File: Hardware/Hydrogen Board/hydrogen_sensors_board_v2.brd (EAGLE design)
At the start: 68.2 x 66 mm, 39 parts, among them U1 ATMEGA328P_TQFP, Y1 16MHz

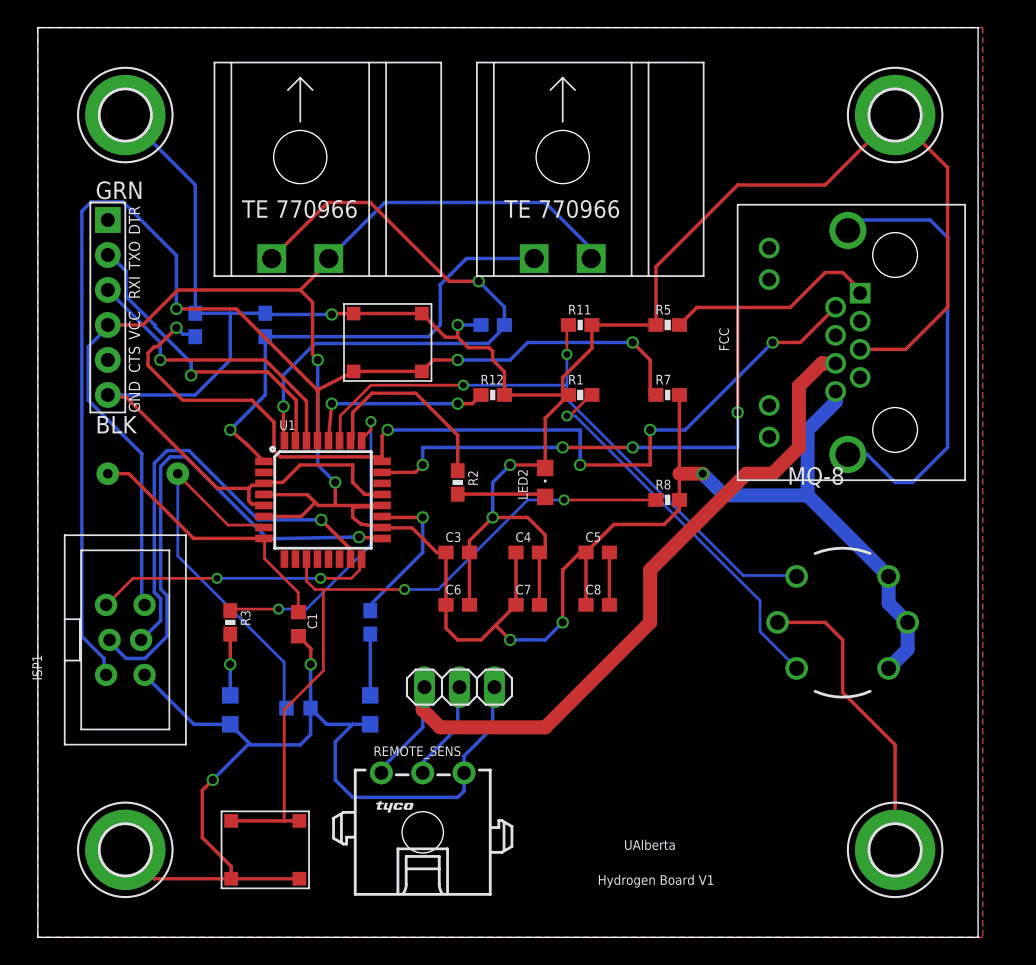
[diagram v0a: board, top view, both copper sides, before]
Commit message: got rid of redundant ground traces
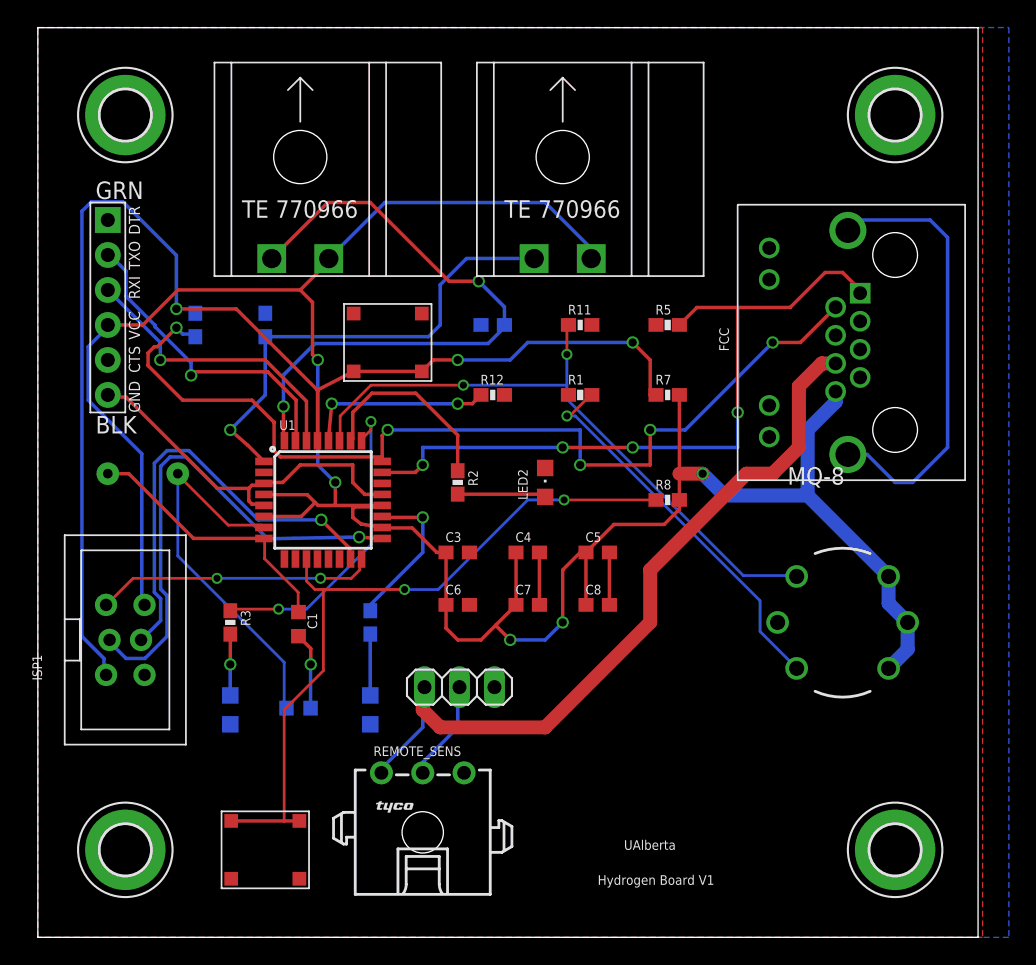
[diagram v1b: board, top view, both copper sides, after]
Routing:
- net GND: track 281.6 -> 40.4 mm, vias 6 -> 1

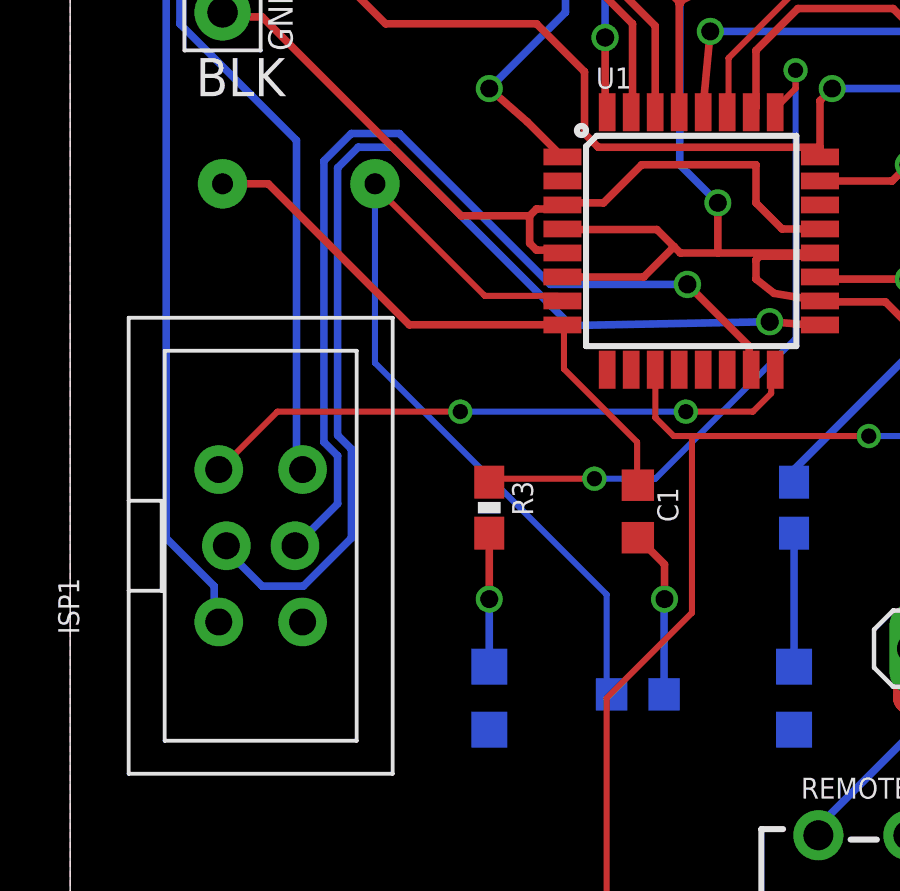
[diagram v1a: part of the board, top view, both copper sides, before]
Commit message: removed more useless ground traces. Moved caps for xtal closer to the actual crystal
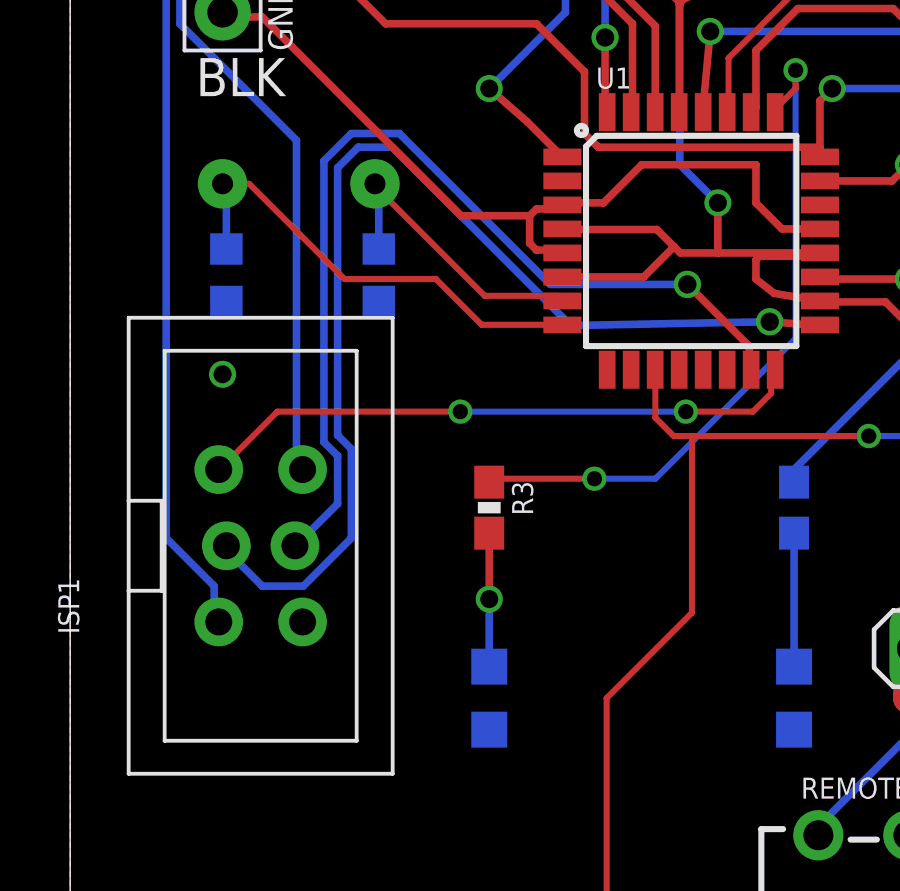
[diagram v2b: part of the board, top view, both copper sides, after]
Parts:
- moved C2 16.4 mm to (10.3, 30.6), turned to 270 degrees
- moved C1 15.8 mm to (5.21, 30.6), flipped to the bottom
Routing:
- net N$1: track 28.2 -> 10.1 mm
- net GND: track 40.4 -> 34.8 mm
- net N$3: track 19.7 -> 15.5 mm
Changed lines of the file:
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@@
 <setting verticaltext="up"/>
 </settings>
-<grid distance="0.025" unitdist="inch" unit="inch" style="lines" multiple="1" display="no" altdistance="0.005" altunitdist="inch" altunit="inch"/>
+<grid distance="0.02" unitdist="inch" unit="inch" style="lines" multiple="1" display="no" altdistance="0.005" altunitdist="inch" altunit="inch"/>
 <layers>
 <layer number="1" name="Top" color="4" fill="1" visible="yes" active="yes"/>
@@
 </autorouter>
 <elements>
-<element name="C1" library="adafruit" package="C0603K" value="22pF" x="18.923" y="22.733" smashed="yes" rot="R270">
-<attribute name="NAME" x="19.573" y="23.533" size="0.7" layer="25" ratio="15" rot="R270"/>
-</element>
-<element name="C2" library="adafruit" package="C0603K" value="22pF" x="18.923" y="16.637" smashed="yes" rot="MR180">
-<attribute name="NAME" x="18.123" y="15.987" size="0.7" layer="26" ratio="15" rot="MR180"/>
+<element name="C1" library="adafruit" package="C0603K" value="22pF" x="5.207" y="30.607" smashed="yes" rot="MR270">
+<attribute name="NAME" x="4.557" y="31.407" size="0.7" layer="26" ratio="15" rot="MR270"/>
+</element>
+<element name="C2" library="adafruit" package="C0603K" value="22pF" x="10.287" y="30.607" smashed="yes" rot="MR270">
+<attribute name="NAME" x="9.637" y="31.407" size="0.7" layer="26" ratio="15" rot="MR270"/>
 </element>
 <element name="ETH1" library="ETHERNET" package="A122645-ND" value="FCC" x="62.23" y="43.18" smashed="yes" rot="R90">
@@
 <contactref element="C3" pad="2"/>
 <wire x1="41.49" y1="27.94" x2="41.49" y2="24.13" width="0.254" layer="1"/>
-<wire x1="19.798" y1="16.637" x2="19.798" y2="19.798" width="0.254" layer="16"/>
-<wire x1="19.798" y1="19.798" x2="19.812" y2="19.812" width="0.254" layer="16"/>
-<via x="19.812" y="19.812" extent="1-16" drill="0.6"/>
-<wire x1="19.812" y1="19.812" x2="19.812" y2="20.969" width="0.254" layer="1"/>
-<wire x1="19.812" y1="20.969" x2="18.923" y2="21.858" width="0.254" layer="1"/>
 <wire x1="36.41" y1="24.13" x2="36.41" y2="27.94" width="0.254" layer="1"/>
 <polygon width="0.4064" layer="1" isolate="0.3048">
@@
 <vertex x="70.485" y="0"/>
 </polygon>
-<wire x1="59.69" y1="42.68" x2="62.23" y2="59.69" width="0" layer="19" extent="1-1"/>
-<wire x1="44.87" y1="44.45" x2="59.69" y2="42.68" width="0" layer="19" extent="1-1"/>
-<wire x1="40.22" y1="44.45" x2="44.87" y2="44.45" width="0" layer="19" extent="1-1"/>
-<wire x1="38.52" y1="39.37" x2="40.22" y2="44.45" width="0" layer="19" extent="1-1"/>
-<wire x1="33.87" y1="39.37" x2="38.52" y2="39.37" width="0" layer="19" extent="1-1"/>
-<wire x1="32.17" y1="44.45" x2="33.87" y2="39.37" width="0" layer="19" extent="1-16"/>
-<wire x1="27.875" y1="45.28" x2="32.17" y2="44.45" width="0" layer="19" extent="1-16"/>
-<wire x1="22.925" y1="45.28" x2="27.875" y2="45.28" width="0" layer="19" extent="1-1"/>
-<wire x1="36.83" y1="34.07" x2="38.52" y2="39.37" width="0" layer="19" extent="1-1"/>
-<wire x1="36.41" y1="27.94" x2="36.83" y2="34.07" width="0" layer="19" extent="1-1"/>
-<wire x1="41.49" y1="27.94" x2="36.41" y2="27.94" width="0" layer="19" extent="1-1"/>
-<wire x1="31.33" y1="27.94" x2="36.41" y2="27.94" width="0" layer="19" extent="1-1"/>
-<wire x1="31.33" y1="24.13" x2="31.33" y2="27.94" width="0" layer="19" extent="1-1"/>
-<wire x1="33.147" y1="18.161" x2="31.33" y2="24.13" width="0" layer="19" extent="1-1"/>
-<wire x1="16.51" y1="45.3" x2="22.925" y2="45.28" width="0" layer="19" extent="1-16"/>
-<wire x1="11.43" y1="45.3" x2="16.51" y2="45.3" width="0" layer="19" extent="16-16"/>
-<wire x1="30.94" y1="11.94" x2="33.147" y2="18.161" width="0" layer="19" extent="1-1"/>
-<wire x1="24.9936" y1="32.15" x2="31.33" y2="27.94" width="0" layer="19" extent="1-1"/>
-<wire x1="24.13" y1="15.46" x2="30.94" y2="11.94" width="0" layer="19" extent="16-16"/>
-<wire x1="19.798" y1="16.637" x2="24.13" y2="15.46" width="0" layer="19" extent="16-16"/>
-<wire x1="13.97" y1="15.46" x2="19.798" y2="16.637" width="0" layer="19" extent="16-16"/>
-<wire x1="7.747" y1="19.05" x2="13.97" y2="15.46" width="0" layer="19" extent="16-16"/>
-<wire x1="14.035" y1="4.25" x2="13.97" y2="15.46" width="0" layer="19" extent="1-16"/>
-<wire x1="18.985" y1="4.25" x2="14.035" y2="4.25" width="0" layer="19" extent="1-1"/>
-<wire x1="6.35" y1="6.35" x2="14.035" y2="4.25" width="0" layer="19" extent="1-1"/>
-<wire x1="53.7" y1="22.86" x2="41.49" y2="24.13" width="0" layer="19" extent="1-1"/>
-<wire x1="6.35" y1="59.69" x2="11.43" y2="45.3" width="0" layer="19" extent="16-16"/>
-<wire x1="62.23" y1="6.35" x2="53.7" y2="22.86" width="0" layer="19" extent="1-1"/>
+<via x="5.08" y="27.305" extent="1-16" drill="0.6" diameter="0.75"/>
 </signal>
 <signal name="N$2">
@@
 <contactref element="U1" pad="7"/>
 <contactref element="C2" pad="1"/>
-<wire x1="17.8816" y1="19.9644" x2="17.8816" y2="16.7132" width="0.2032" layer="16"/>
-<wire x1="10.16" y1="27.686" x2="17.8816" y2="19.9644" width="0.2032" layer="16"/>
-<wire x1="10.16" y1="33.655" x2="10.16" y2="27.686" width="0.2032" layer="16"/>
-<wire x1="17.8816" y1="16.7132" x2="18.048" y2="16.637" width="0.2032" layer="16"/>
 <wire x1="13.8176" y1="29.9212" x2="16.256" y2="29.9212" width="0.2032" layer="1"/>
 <wire x1="10.16" y1="33.5788" x2="13.8176" y2="29.9212" width="0.2032" layer="1"/>
 <wire x1="16.256" y1="29.9212" x2="16.4084" y2="29.75" width="0.2032" layer="1"/>
 <wire x1="10.16" y1="33.5788" x2="10.16" y2="33.655" width="0.2032" layer="1"/>
+<wire x1="10.287" y1="31.482" x2="10.287" y2="33.528" width="0.254" layer="16"/>
+<wire x1="10.287" y1="33.528" x2="10.16" y2="33.655" width="0.254" layer="16"/>
 </signal>
 <signal name="N$3">
@@
 <contactref element="Y1" pad="1"/>
 <contactref element="C1" pad="1"/>
-<wire x1="5.08" y1="33.655" x2="6.604" y2="33.655" width="0.254" layer="1"/>
-<wire x1="6.604" y1="33.655" x2="11.303" y2="28.956" width="0.254" layer="1"/>
-<wire x1="11.303" y1="28.956" x2="16.4024" y2="28.956" width="0.254" layer="1"/>
-<wire x1="16.4024" y1="28.956" x2="16.4084" y2="28.95" width="0.254" layer="1"/>
-<wire x1="18.8976" y1="25.0444" x2="18.8976" y2="23.622" width="0.2032" layer="1"/>
-<wire x1="16.4592" y1="27.4828" x2="18.8976" y2="25.0444" width="0.2032" layer="1"/>
-<wire x1="16.4592" y1="28.9052" x2="16.4592" y2="27.4828" width="0.2032" layer="1"/>
-<wire x1="18.8976" y1="23.622" x2="18.923" y2="23.608" width="0.2032" layer="1"/>
-<wire x1="16.4592" y1="28.9052" x2="16.4084" y2="28.95" width="0.2032" layer="1"/>
+<wire x1="5.207" y1="31.482" x2="5.207" y2="33.528" width="0.254" layer="16"/>
+<wire x1="5.207" y1="33.528" x2="5.08" y2="33.655" width="0.254" layer="16"/>
+<wire x1="5.08" y1="33.655" x2="5.969" y2="33.655" width="0.2032" layer="1"/>
+<wire x1="5.969" y1="33.655" x2="9.144" y2="30.48" width="0.2032" layer="1"/>
+<wire x1="9.144" y1="30.48" x2="12.192" y2="30.48" width="0.2032" layer="1"/>
+<wire x1="12.192" y1="30.48" x2="13.716" y2="28.956" width="0.2032" layer="1"/>
+<wire x1="13.716" y1="28.956" x2="16.4024" y2="28.956" width="0.2032" layer="1"/>
+<wire x1="16.4024" y1="28.956" x2="16.4084" y2="28.95" width="0.2032" layer="1"/>
 </signal>
 <signal name="ATM_RESET">

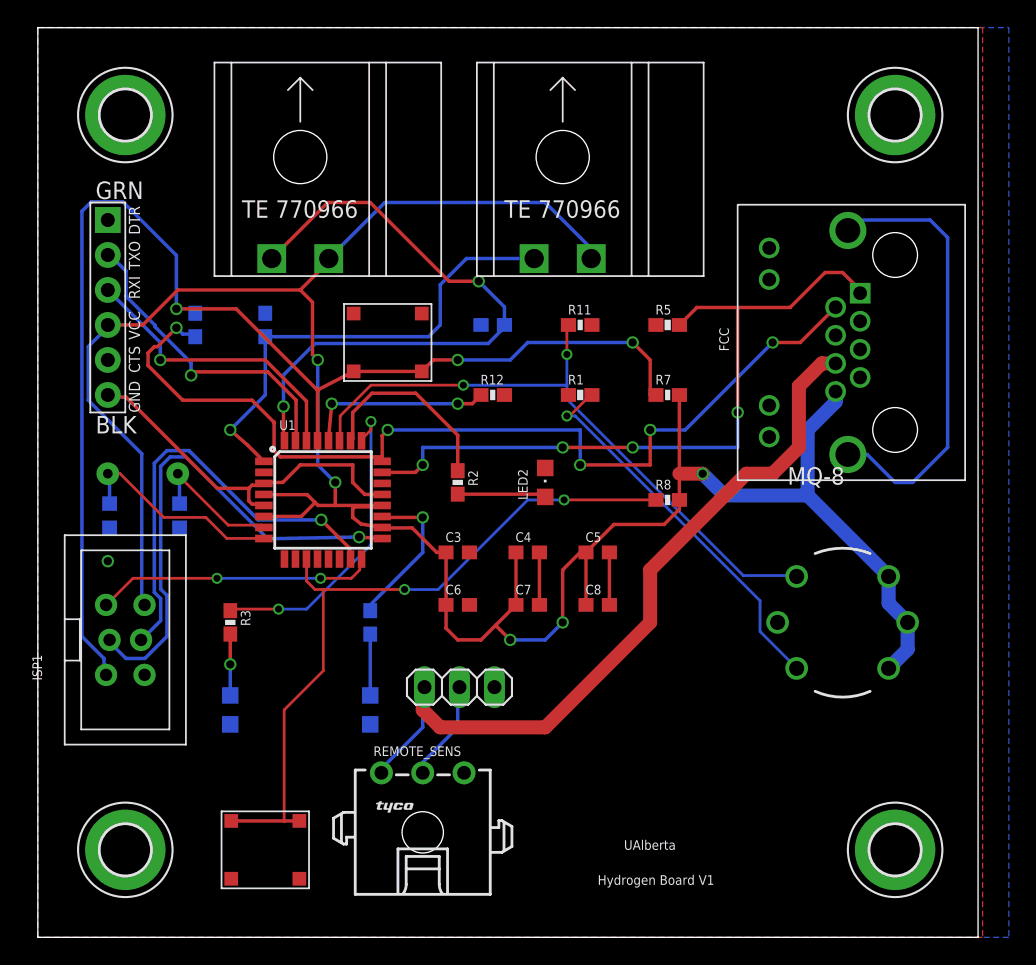
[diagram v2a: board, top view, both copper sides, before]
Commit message: more general clean up. Moved LEDs to top layer. Removed some useless traces. Fixed warnings
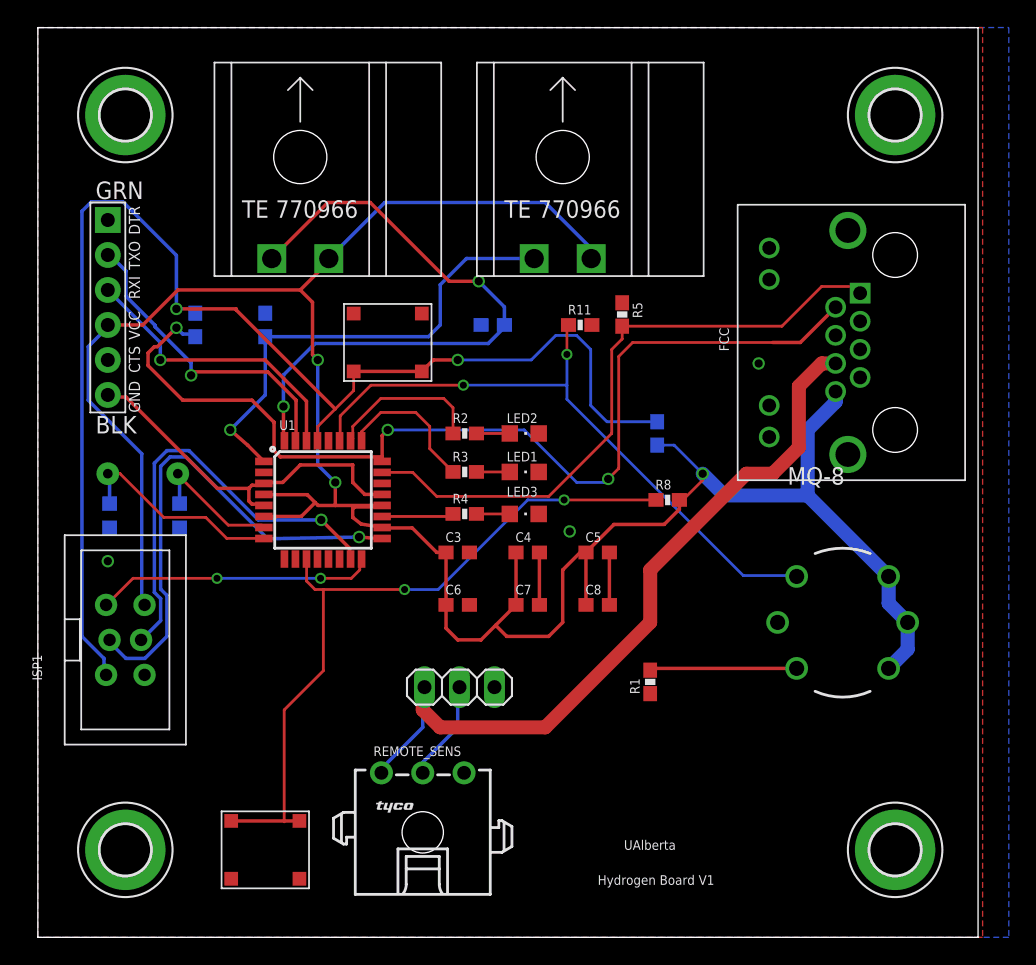
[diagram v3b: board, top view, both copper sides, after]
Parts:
- removed R12: 100k, SparkFun-Resistors:0603-RES
- moved LED1 27.5 mm to (35.3, 33.8), flipped to the top, turned to 270 degrees
- moved R1 21.4 mm to (44.5, 18.5), turned to 90 degrees
- moved R3 20.2 mm to (31.0, 33.8), turned to 0 degrees
- moved LED3 18.1 mm to (35.3, 30.7), flipped to the top, turned to 270 degrees
- moved R4 10.4 mm to (31.0, 30.7), flipped to the top, turned to 0 degrees
- moved LED2 3.87 mm to (35.3, 36.6), turned to 270 degrees
- moved R2 3.59 mm to (31.0, 36.6), turned to 0 degrees
- moved R5 3.39 mm to (42.4, 45.2), turned to 270 degrees
- moved R7 2.90 mm to (45.0, 36.6), flipped to the bottom, turned to 270 degrees
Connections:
- removed net H2OUT_2: R12.1, U1.28
- removed net N$10: ETH1.P$13, ETH1.P$14
- removed net N$16: ETH1.P$3
- removed net N$22: ETH1.P$10
- removed net N$23: ETH1.P$9
- removed net N$24: ETH1.P$12
- removed net N$25: ETH1.P$11
- net GND: now also ETH1.P$13, ETH1.P$14; no longer R12.2
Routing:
- net N$10: track 32.5 -> 0.00 mm
- net N$2: track 28.0 -> 10.7 mm, vias 1 -> 0
- net H2OUT_2: track 13.8 -> 0.00 mm, vias 2 -> 0
- net N$4: track 22.8 -> 10.6 mm, vias 2 -> 0
- net H2_OK: track 52.9 -> 46.0 mm, vias 4 -> 0
- net N$6: track 11.3 -> 5.22 mm, vias 1 -> 0
- net N$8: track 6.43 -> 2.42 mm
- net ATM_RESET: track 92.4 -> 95.9 mm, vias 3 -> 2
- net EXTRA_SIG: track 70.2 -> 73.0 mm, vias 5 -> 3
- net N$5: track 14.2 -> 11.4 mm
- net +5V: track 186.4 -> 183.9 mm, vias 5 -> 3
- net N$9: track 4.45 -> 2.42 mm
- net N$7: track 4.45 -> 2.42 mm, vias 1 -> 0
- net GND: vias 1 -> 3
